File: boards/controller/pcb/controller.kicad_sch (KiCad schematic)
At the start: 10 parts, among them J1 USB_C_Receptacle, SW1 SW_Push, U1 TCPP01-M12, U2 ISZ065N03L5SATMA1, U3 STM32U575RITx, Y1 Crystal

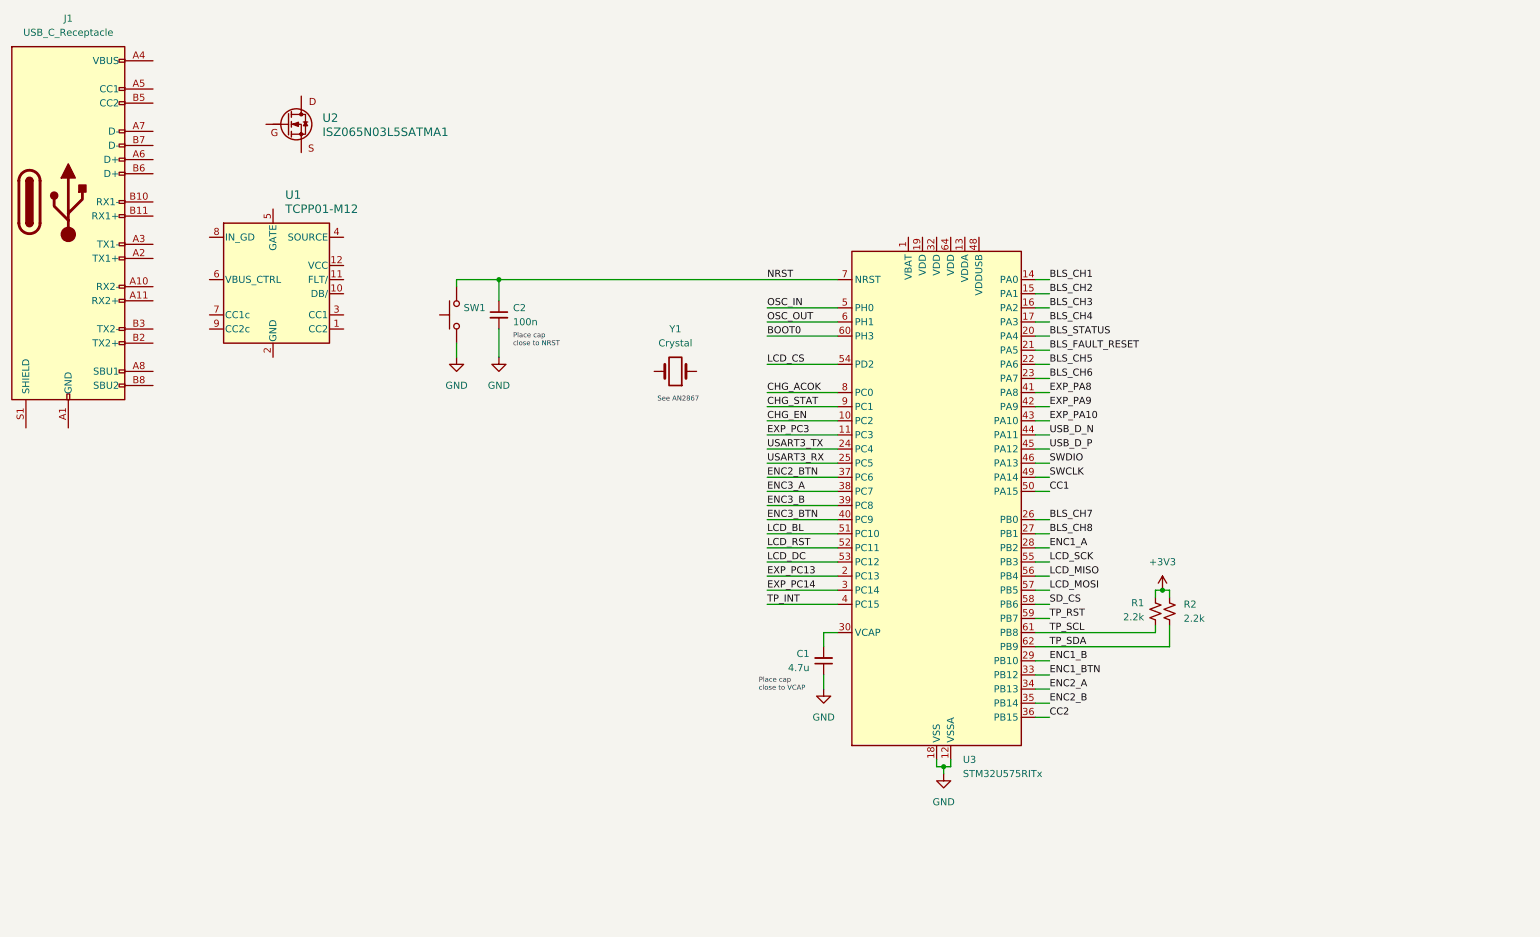
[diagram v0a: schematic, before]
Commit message: controller: Update PCB
Signed-off-by: Nicholas Loehrke <nicholasnloehrke@gmail.com>
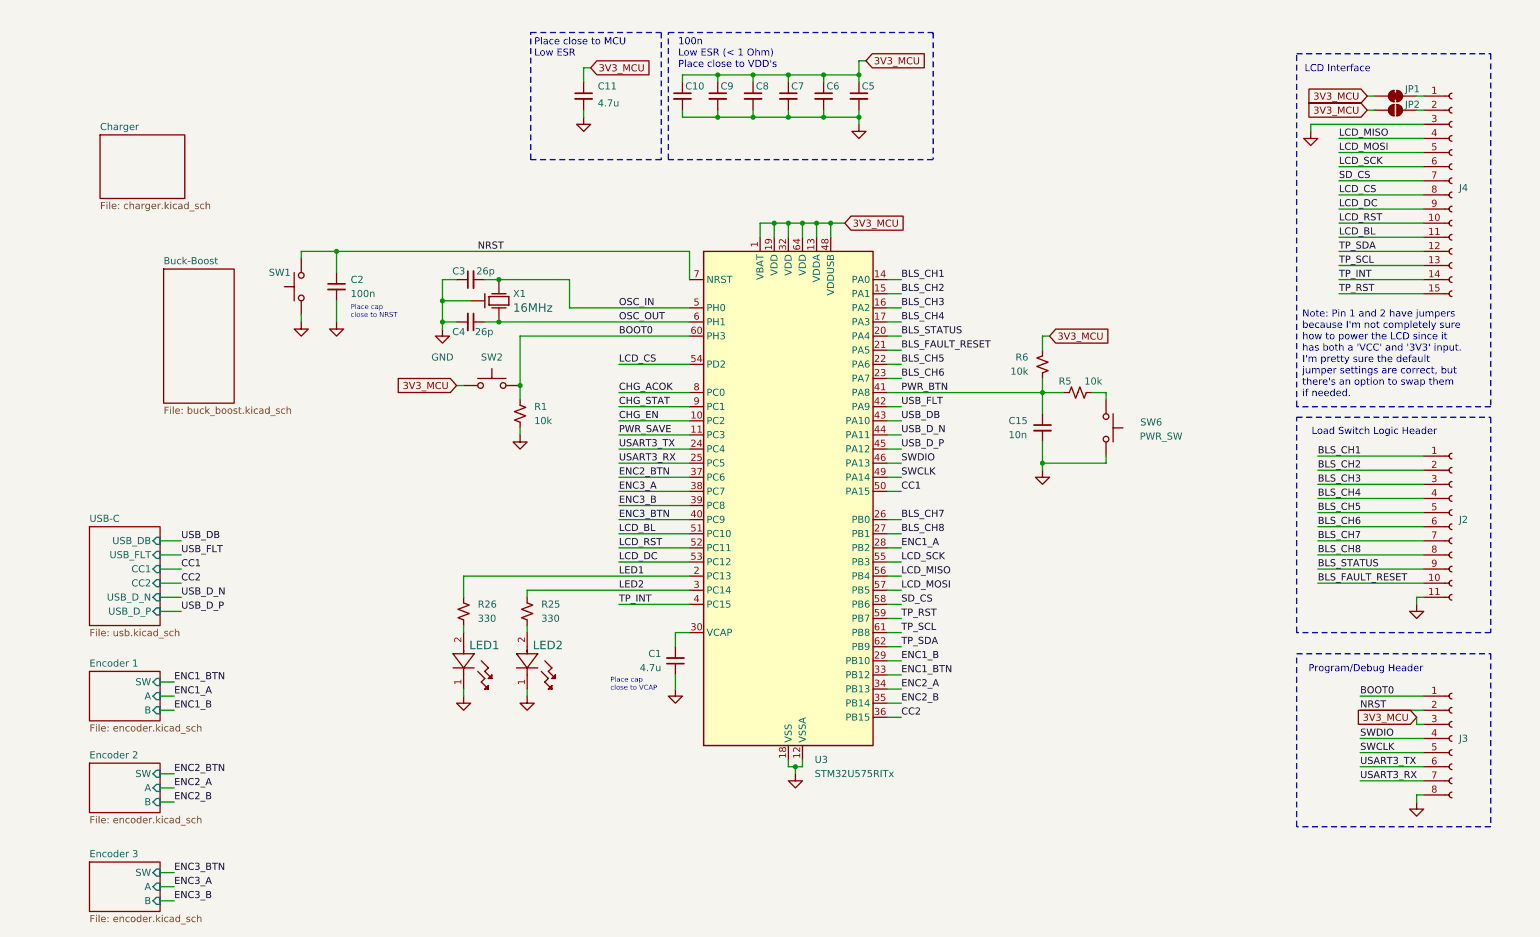
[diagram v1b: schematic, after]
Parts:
- removed J1: USB_C_Receptacle, symbol Connector:USB_C_Receptacle
- removed R2: 2.2k, symbol Device:R_Small_US
- removed U1: TCPP01-M12, QFN12_TCPP01-M12_STM, symbol TCPP01-M12:TCPP01-M12
- removed U2: ISZ065N03L5SATMA1, PG-TSDSON-8-25, symbol ISZ065N03L5SATMA1:ISZ065N03L5SATMA1
- removed Y1: Crystal, symbol Device:Crystal
- added C10, C5, C6, C7, C8, C9: 100n, symbol Device:C_Small
- added C11: 4.7u, symbol Device:C_Small
- added C15: 10n, symbol Device:C_Small
- added C3, C4: 26p, symbol Device:C_Small
- added J2: Conn_01x11_Socket, symbol Connector:Conn_01x11_Socket
- added J3: Conn_01x08_Socket, symbol Connector:Conn_01x08_Socket
- added J4: Conn_01x15_Socket, symbol Connector:Conn_01x15_Socket
- added JP1: SolderJumper_2_Bridged, symbol Jumper:SolderJumper_2_Bridged
- added JP2: SolderJumper_2_Open, symbol Jumper:SolderJumper_2_Open
- added LED1, LED2: B1911PG--20D000514U1930, LED_B1911PG--20D000514U1930_HVK, symbol B1911PG__20D000514U1930:B1911PG--20D000514U1930
- added R25, R26: 330, symbol Device:R_Small_US
- added R5, R6: 10k, symbol Device:R_Small_US
- added SW2: SW_Push, symbol Switch:SW_Push
- added SW6: PWR_SW, symbol Switch:SW_Push
- added X1: 16MHz, RH100-16.000-18-2030-EXT-TR_RAL, symbol RH100-16.000-18-2030-EXT-TR:RH100-16.000-18-2030-EXT-TR
- R1: value 2.2k -> 10k
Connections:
- net +3V3 is gone; now on net BOOT0: R1.1
- net BLS_CH1: now also J2.1 (Pin_1)
- net BLS_CH2: now also J2.2 (Pin_2)
- net BLS_CH3: now also J2.3 (Pin_3)
- net BLS_CH4: now also J2.4 (Pin_4)
- net BLS_CH5: now also J2.5 (Pin_5)
- net BLS_CH6: now also J2.6 (Pin_6)
- net BLS_CH7: now also J2.7 (Pin_7)
- net BLS_CH8: now also J2.8 (Pin_8)
- net BLS_FAULT_RESET: now also J2.10 (Pin_10)
- net BLS_STATUS: now also J2.9 (Pin_9)
- net BOOT0: now also J3.1 (Pin_1), SW2.2
- net GND: now also R1.2, C10.2, C11.2, C15.2, C3.1, C4.2, C5.2, C6.2, C7.2, C8.2, C9.2, J2.11 (Pin_11), J3.8 (Pin_8), J4.3 (Pin_3), LED1.1, LED2.1, SW6.2, X1.2, X1.4
- net LCD_BL: now also J4.11 (Pin_11)
- net LCD_CS: now also J4.8 (Pin_8)
- net LCD_DC: now also J4.9 (Pin_9)
- net LCD_MISO: now also J4.4 (Pin_4)
- net LCD_MOSI: now also J4.5 (Pin_5)
- net LCD_RST: now also J4.10 (Pin_10)
- net LCD_SCK: now also J4.6 (Pin_6)
- net NRST: now also J3.2 (Pin_2)
- net OSC_IN: now also C3.2, X1.1
- net OSC_OUT: now also C4.1, X1.3
- net SD_CS: now also J4.7 (Pin_7)
- net SWCLK: now also J3.5 (Pin_5)
- net SWDIO: now also J3.4 (Pin_4)
- net TP_INT: now also J4.14 (Pin_14)
- net TP_RST: now also J4.15 (Pin_15)
- net TP_SCL: now also J4.13 (Pin_13); no longer R1.2
- net TP_SDA: now also J4.12 (Pin_12)
- net USART3_RX: now also J3.7 (Pin_7)
- net USART3_TX: now also J3.6 (Pin_6)
- net 3V3_MCU: now reaches U3.1 (VBAT)
- net 3V3_MCU: now also U3.13 (VDDA), U3.19 (VDD), U3.32 (VDD), U3.48 (VDDUSB), U3.64 (VDD), C10.1, C11.1, C5.1, C6.1, C7.1, C8.1, C9.1, J3.3 (Pin_3), JP1.1 (A), JP2.1 (A), R6.1, SW2.1
- net EXP_PA10 renamed USB_DB
- net EXP_PA8 renamed PWR_BTN
- net PWR_BTN: now also C15.1, R5.1, R6.2
- net EXP_PA9 renamed USB_FLT
- net EXP_PC13 renamed LED1
- net LED1: now also R26.1
- net EXP_PC14 renamed LED2
- net LED2: now also R25.1
- net EXP_PC3 renamed PWR_SAVE
- new net: LED2.2, R25.2
- new net: R5.2, SW6.1
- new net: LED1.2, R26.2
- new net: J4.2 (Pin_2), JP2.2 (B)
- new net: J4.1 (Pin_1), JP1.2 (B)
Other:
- added sheet Buck-Boost (buck_boost.kicad_sch)
- added sheet Charger (charger.kicad_sch)
- added sheet Encoder 1 (encoder.kicad_sch)
- added sheet Encoder 2 (encoder.kicad_sch)
- added sheet Encoder 3 (encoder.kicad_sch)
- added sheet USB-C (usb.kicad_sch)
- note added: "100n Low ESR (< 1 Ohm) Place close to VDD's"
- note added: "LCD Interface"
- note added: "Load Switch Logic Header"
- note added: "Note: Pin 1 and 2 have jumpers because I'm not completely sure how to power the LCD since it has both a 'VCC' and '3V3' input. I'm pretty sure the default jumper settings are correct, but there's an option to swap them if needed."
- note added: "Place close to MCU Low ESR"
- note added: "Program/Debug Header"
- note removed: "See AN2867"
- moved on the sheet: C1, C2, SW1, U3

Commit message: controller: Update PCB
Signed-off-by: Nicholas Loehrke <nicholasnloehrke@gmail.com>
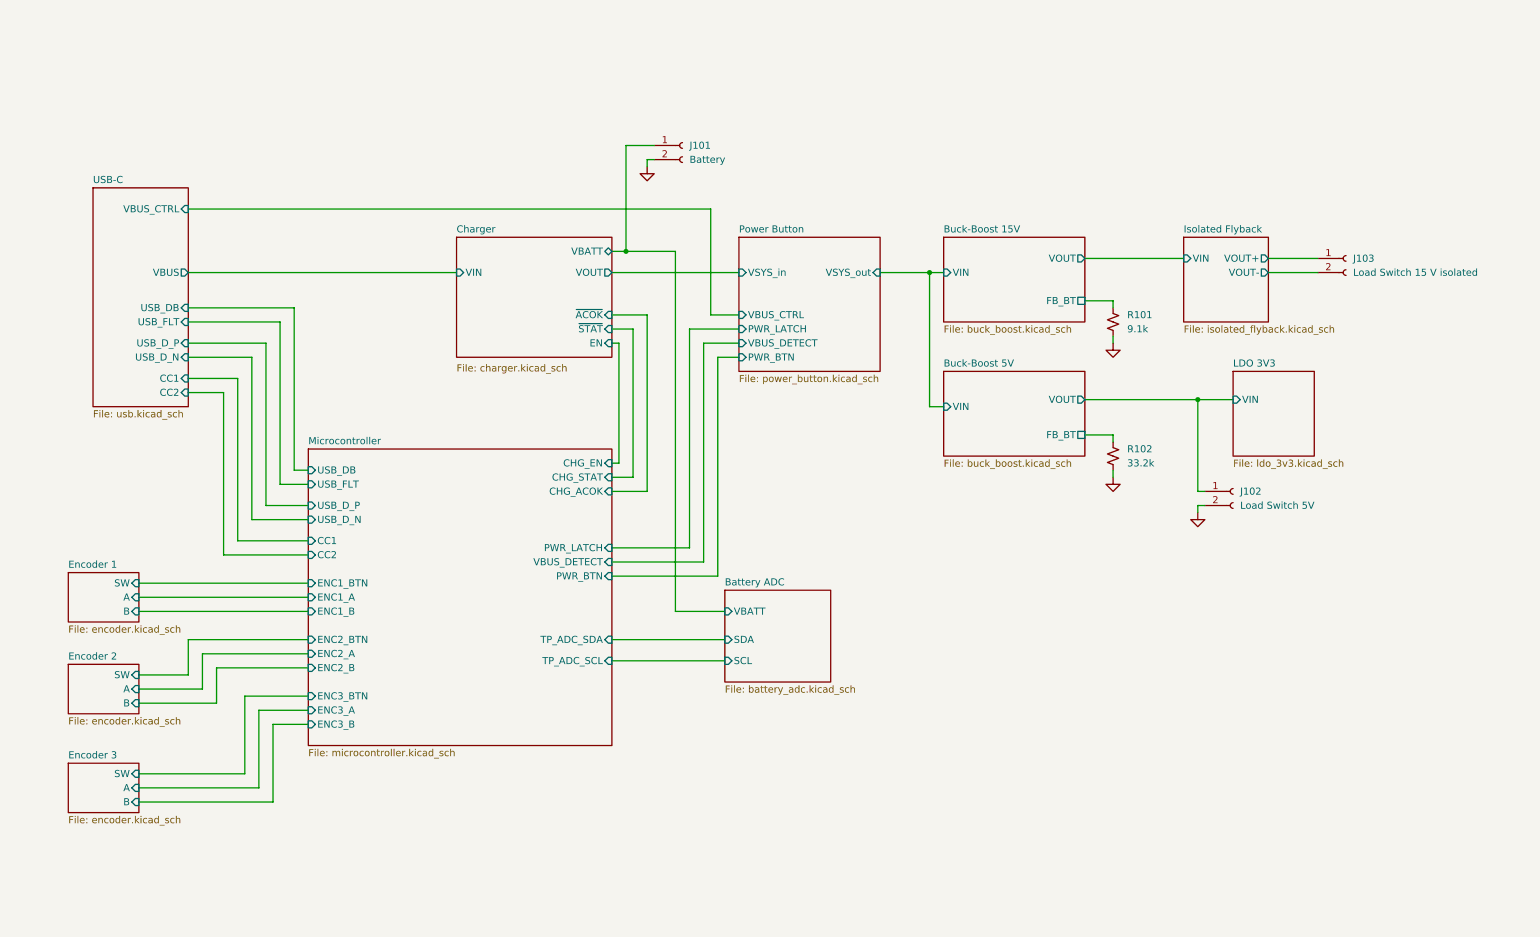
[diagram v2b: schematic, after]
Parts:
- removed C1, C11: 4.7u, symbol Device:C_Small
- removed C10, C2, C5, C6, C7, C8, C9: 100n, symbol Device:C_Small
- removed C15: 10n, symbol Device:C_Small
- removed C3, C4: 26p, symbol Device:C_Small
- removed J2: Conn_01x11_Socket, symbol Connector:Conn_01x11_Socket
- removed J3: Conn_01x08_Socket, symbol Connector:Conn_01x08_Socket
- removed J4: Conn_01x15_Socket, symbol Connector:Conn_01x15_Socket
- removed JP1: SolderJumper_2_Bridged, symbol Jumper:SolderJumper_2_Bridged
- removed JP2: SolderJumper_2_Open, symbol Jumper:SolderJumper_2_Open
- removed LED1, LED2: B1911PG--20D000514U1930, LED_B1911PG--20D000514U1930_HVK, symbol B1911PG__20D000514U1930:B1911PG--20D000514U1930
- removed R1, R5, R6: 10k, symbol Device:R_Small_US
- removed R25, R26: 330, symbol Device:R_Small_US
- removed SW1, SW2: SW_Push, symbol Switch:SW_Push
- removed SW6: PWR_SW, symbol Switch:SW_Push
- removed U3: STM32U575RITx, Package_QFP:LQFP-64_10x10mm_P0.5mm, symbol MCU_ST_STM32U5:STM32U575RITx
- removed X1: 16MHz, RH100-16.000-18-2030-EXT-TR_RAL, symbol RH100-16.000-18-2030-EXT-TR:RH100-16.000-18-2030-EXT-TR
- added J101: Battery, symbol Connector:Conn_01x02_Socket
- added J102: Load Switch 5V, symbol Connector:Conn_01x02_Socket
- added J103: Load Switch 15 V isolated, symbol Connector:Conn_01x02_Socket
- added R101: 9.1k, symbol Device:R_Small_US
- added R102: 33.2k, symbol Device:R_Small_US
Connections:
- net GND: now also J101.2 (Pin_2), J102.2 (Pin_2), R101.2, R102.2
- new net Battery ADC/VBATT: J101.1 (Pin_1)
- new net Buck-Boost 15V/FB_BT: R101.1
- new net Buck-Boost 5V/FB_BT: R102.1
- new net Buck-Boost 5V/VOUT: J102.1 (Pin_1)
- new net Isolated Flyback/VOUT+: J103.1 (Pin_1)
- new net Isolated Flyback/VOUT-: J103.2 (Pin_2)
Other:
- sheet Buck-Boost renamed Buck-Boost 15V
- added sheet Battery ADC (battery_adc.kicad_sch)
- added sheet Buck-Boost 5V (buck_boost.kicad_sch)
- added sheet Isolated Flyback (isolated_flyback.kicad_sch)
- added sheet LDO 3V3 (ldo_3v3.kicad_sch)
- added sheet Microcontroller (microcontroller.kicad_sch)
- added sheet Power Button (power_button.kicad_sch)
- sheet Buck-Boost 15V ports: added FB_BT, VIN, VOUT; removed none
- sheet Charger ports: added EN, VBATT, VIN, VOUT, ~{ACOK}, ~{STAT}; removed none
- sheet USB-C ports: added VBUS, VBUS_CTRL; removed none
- note removed: "100n Low ESR (< 1 Ohm) Place close to VDD's"
- note removed: "LCD Interface"
- note removed: "Load Switch Logic Header"
- note removed: "Note: Pin 1 and 2 have jumpers because I'm not completely sure how to power the LCD since it has both a 'VCC' and '3V3' input. I'm pretty sure the default jumper settings are correct, but there's an option to swap them if needed."
- note removed: "Place cap close to NRST"
- note removed: "Place cap close to VCAP"
- note removed: "Place close to MCU Low ESR"
- note removed: "Program/Debug Header"
